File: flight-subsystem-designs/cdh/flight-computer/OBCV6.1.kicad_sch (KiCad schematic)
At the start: 32 parts, among them J1 Conn_01x03, J2 Conn_01x03, J3 Conn_01x03, J4 Conn_01x03, J5 Conn_01x03, J6 Conn_01x03, J7 Conn_02x26_Odd_Even, J8 Conn_02x26_Odd_Even, U1 BEAGLEBONEBLACK, U3 TCAN337G, U4 MCP7940N-xSN, U6 MAX706RESA+T, U7 TMP36xS

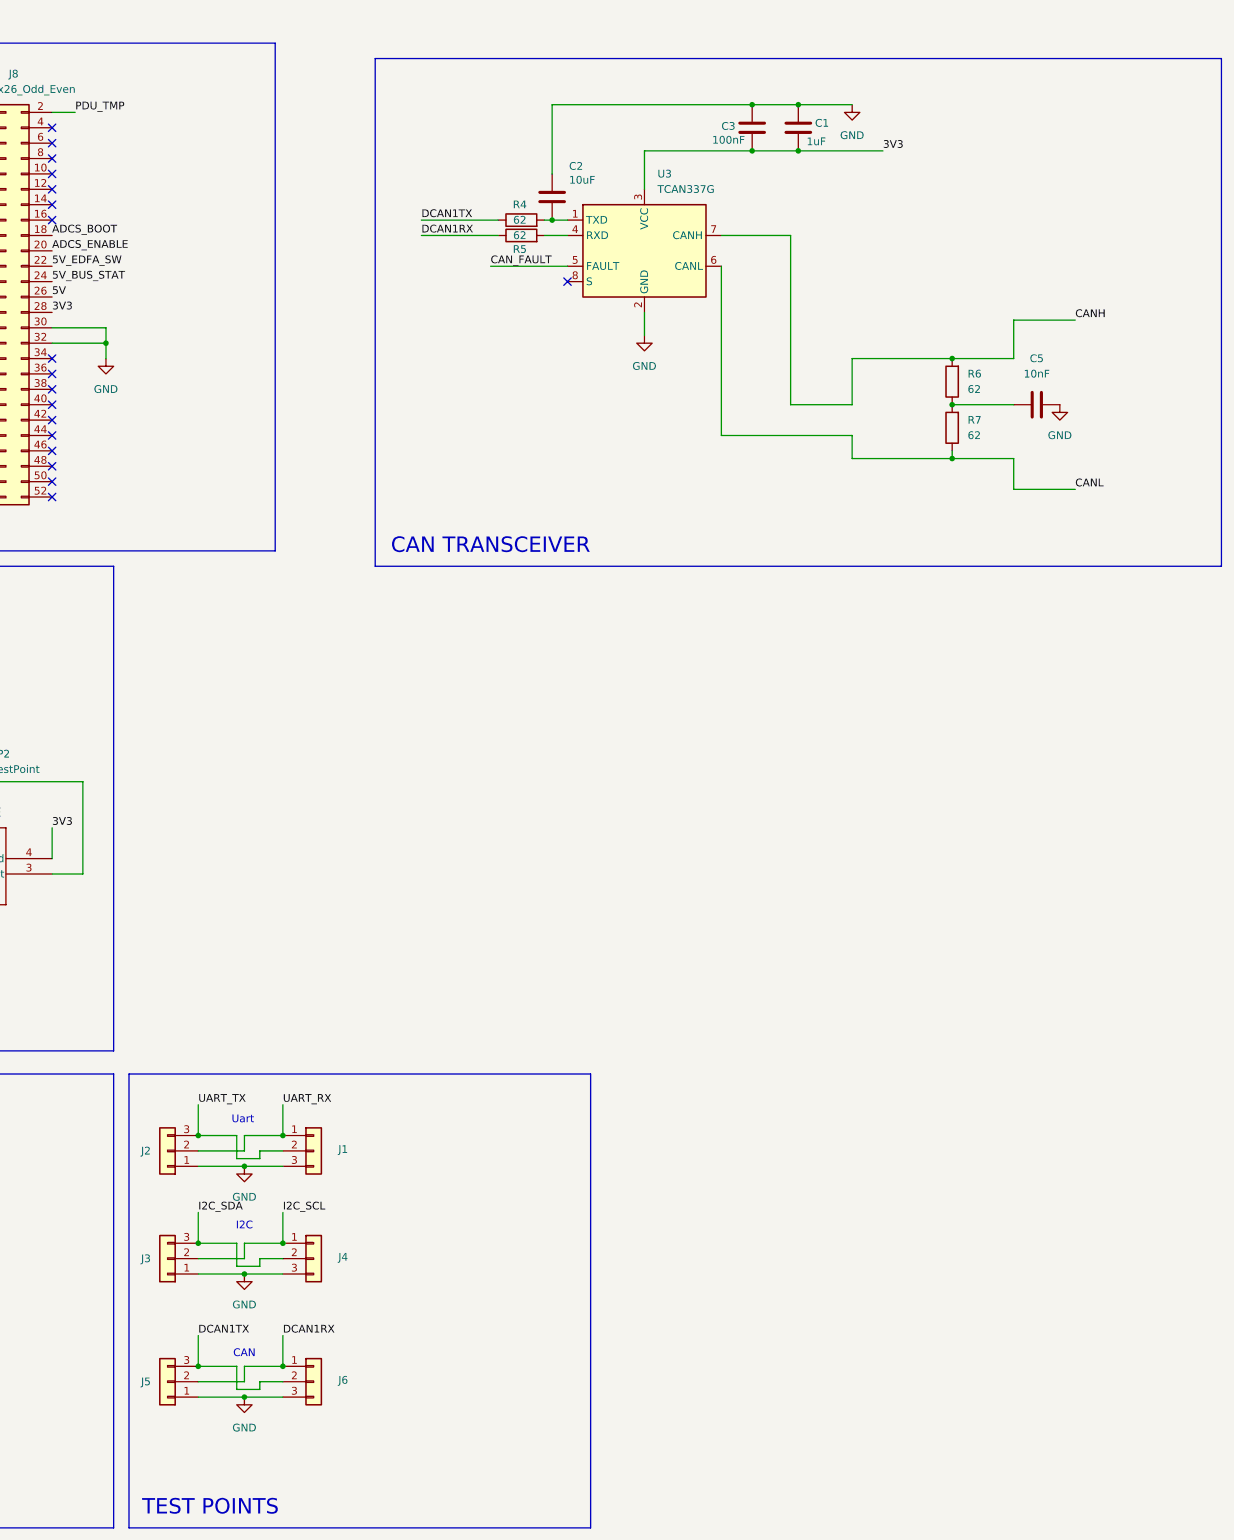
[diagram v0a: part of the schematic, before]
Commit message: Added grounded mounting holes
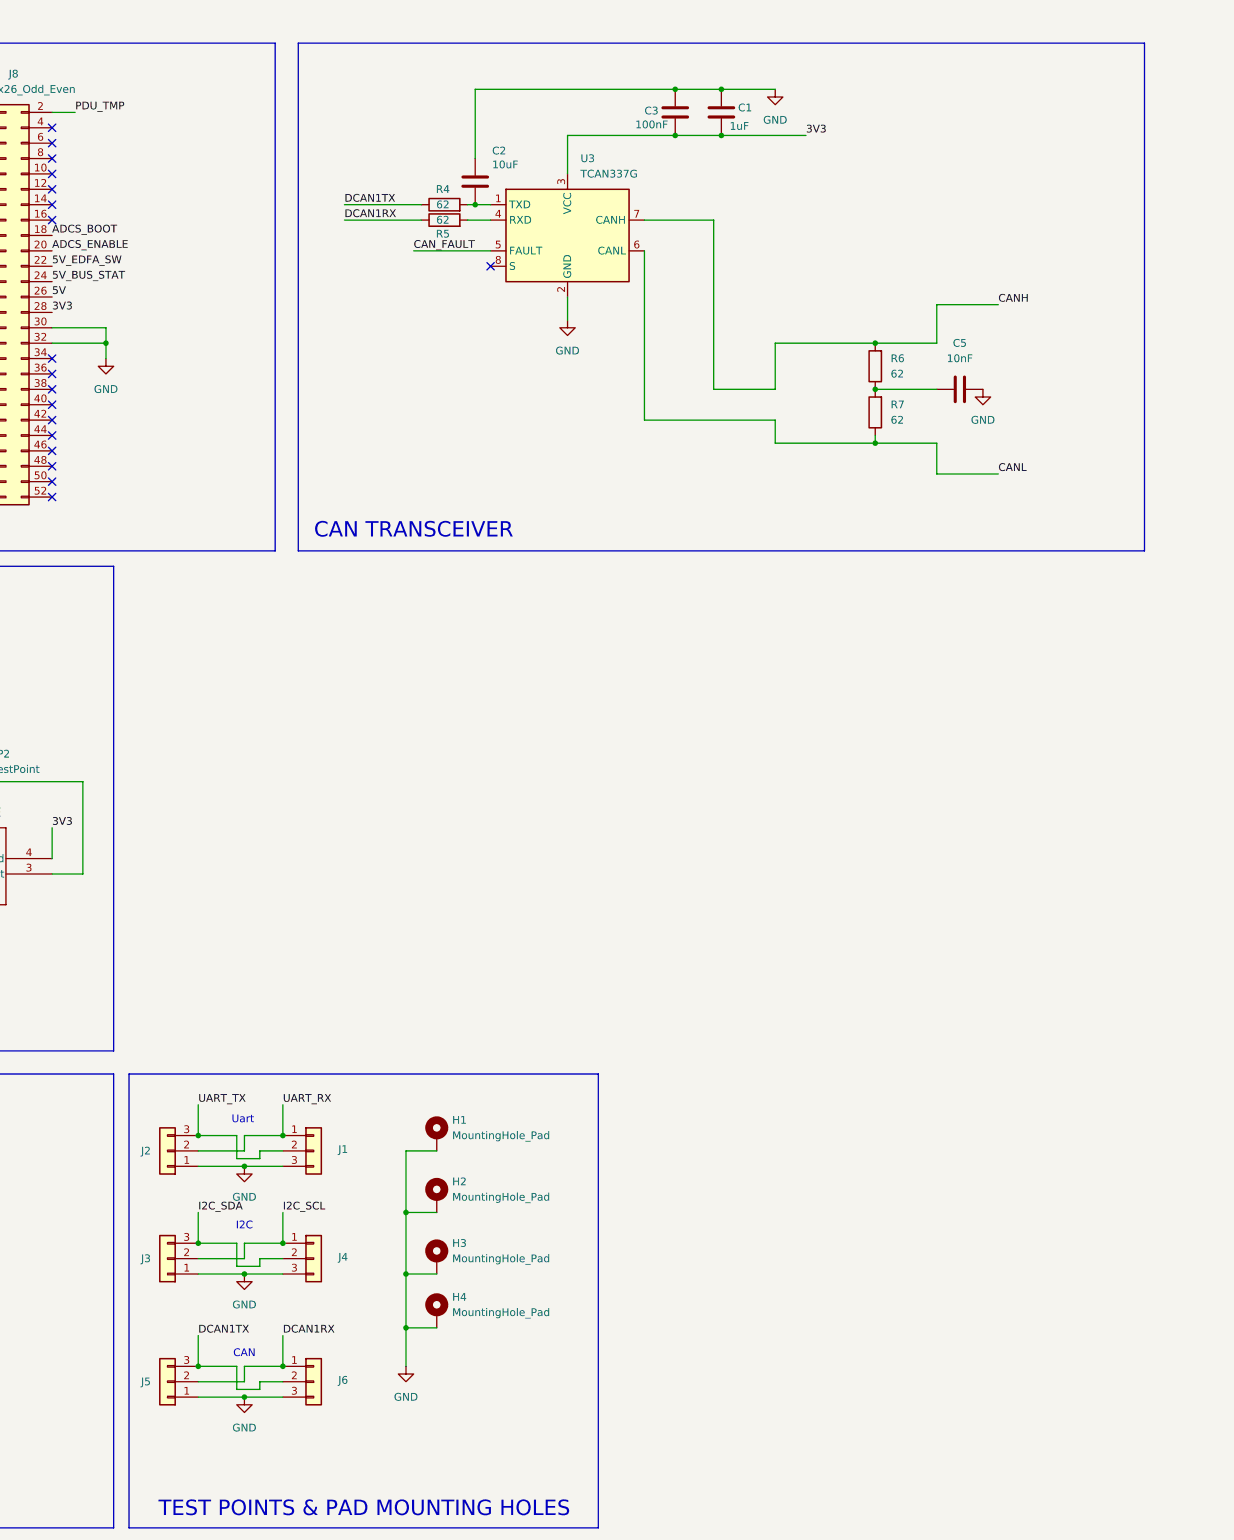
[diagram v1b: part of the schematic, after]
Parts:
- added H1, H2, H3, H4: MountingHole_Pad, symbol Mechanical:MountingHole_Pad
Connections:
- net DGND: now also H1.1, H2.1, H3.1, H4.1
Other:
- note added: "TEST POINTS & PAD MOUNTING HOLES"
- note removed: "TEST POINTS"
- moved on the sheet: C1, C2, C3, C5, R4, R5, R6, R7, U3

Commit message: corrections
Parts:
- J1: footprint Connector_PinHeader_2.54mm:PinHeader_1x03_P2.54mm_Horizontal -> Connector_PinHeader_2.54mm:PinHeader_1x03_P2.54mm_Vertical
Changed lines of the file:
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@@
 			)
 		)
-		(property "Footprint" "Connector_PinHeader_2.54mm:PinHeader_1x03_P2.54mm_Horizontal"
+		(property "Footprint" "Connector_PinHeader_2.54mm:PinHeader_1x03_P2.54mm_Vertical"
 			(at 264.16 196.85 0)
 			(effects

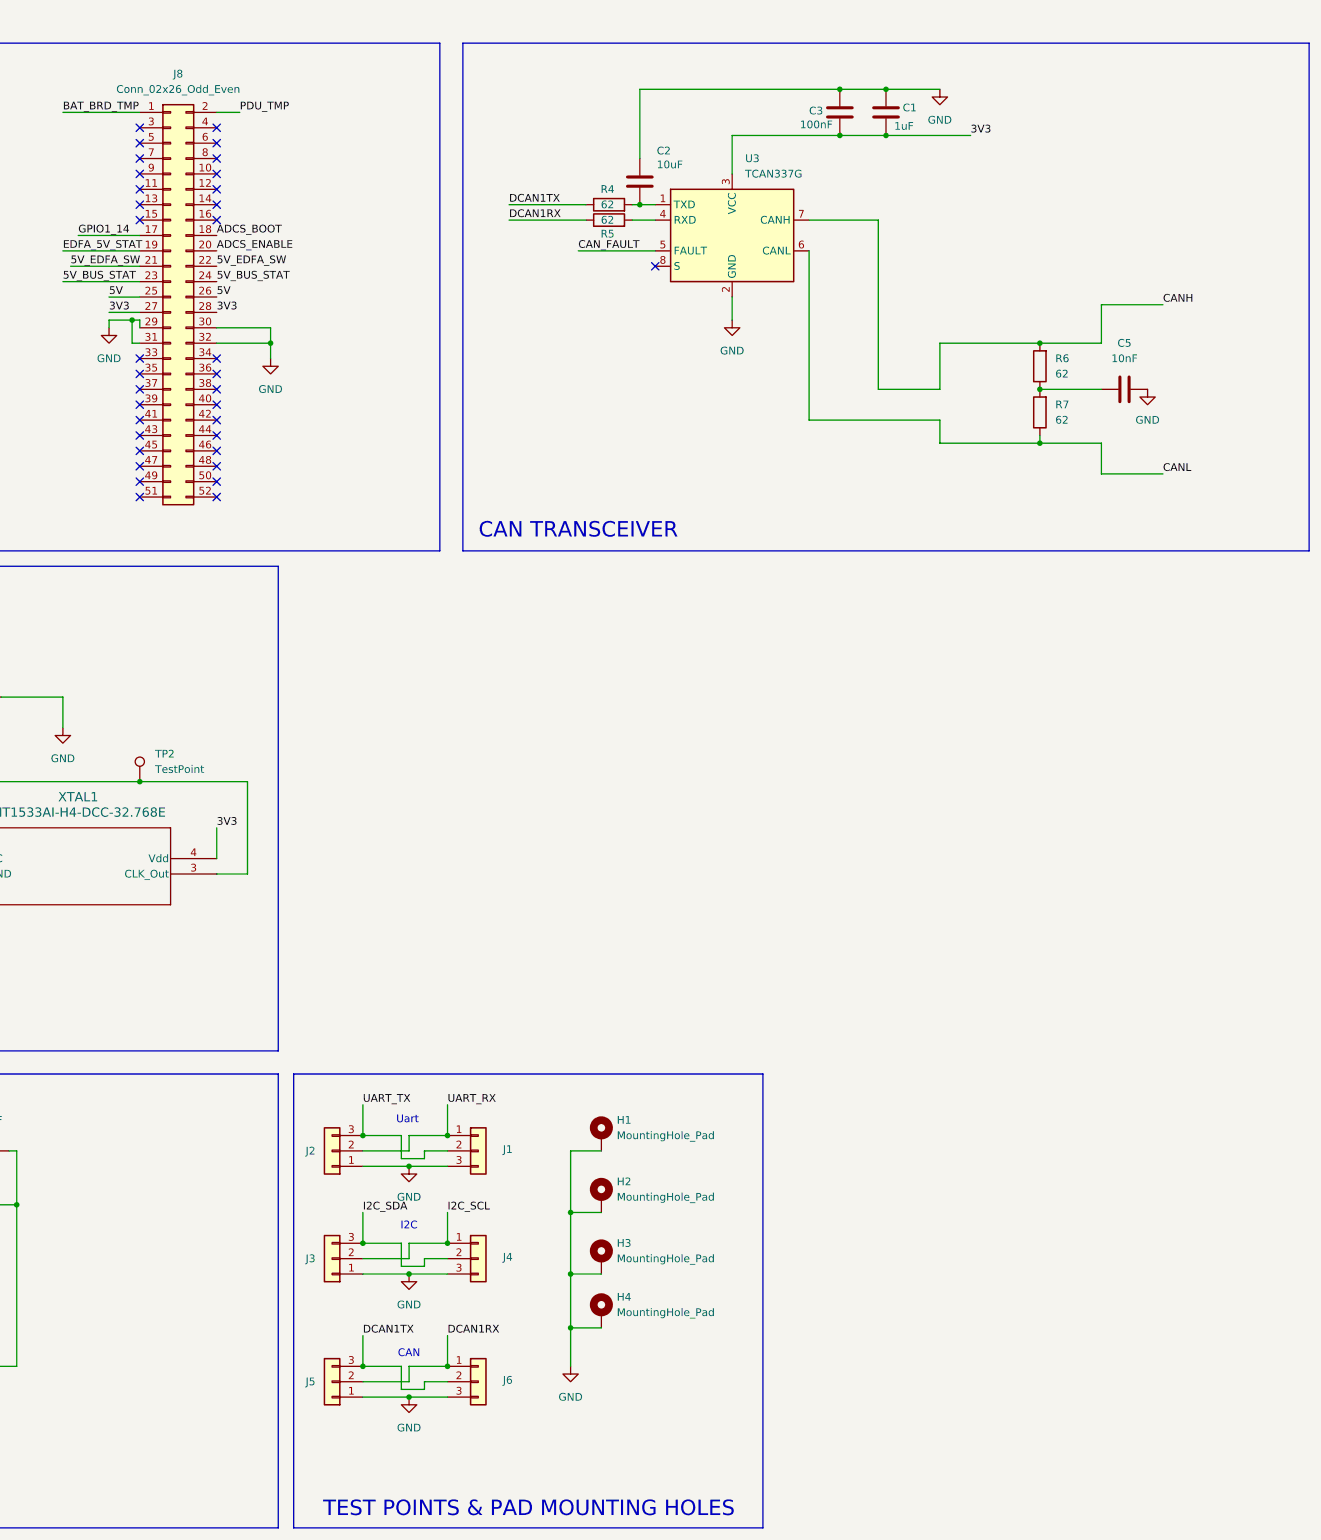
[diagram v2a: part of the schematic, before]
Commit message: Added overvoltage regulation, *check J8*
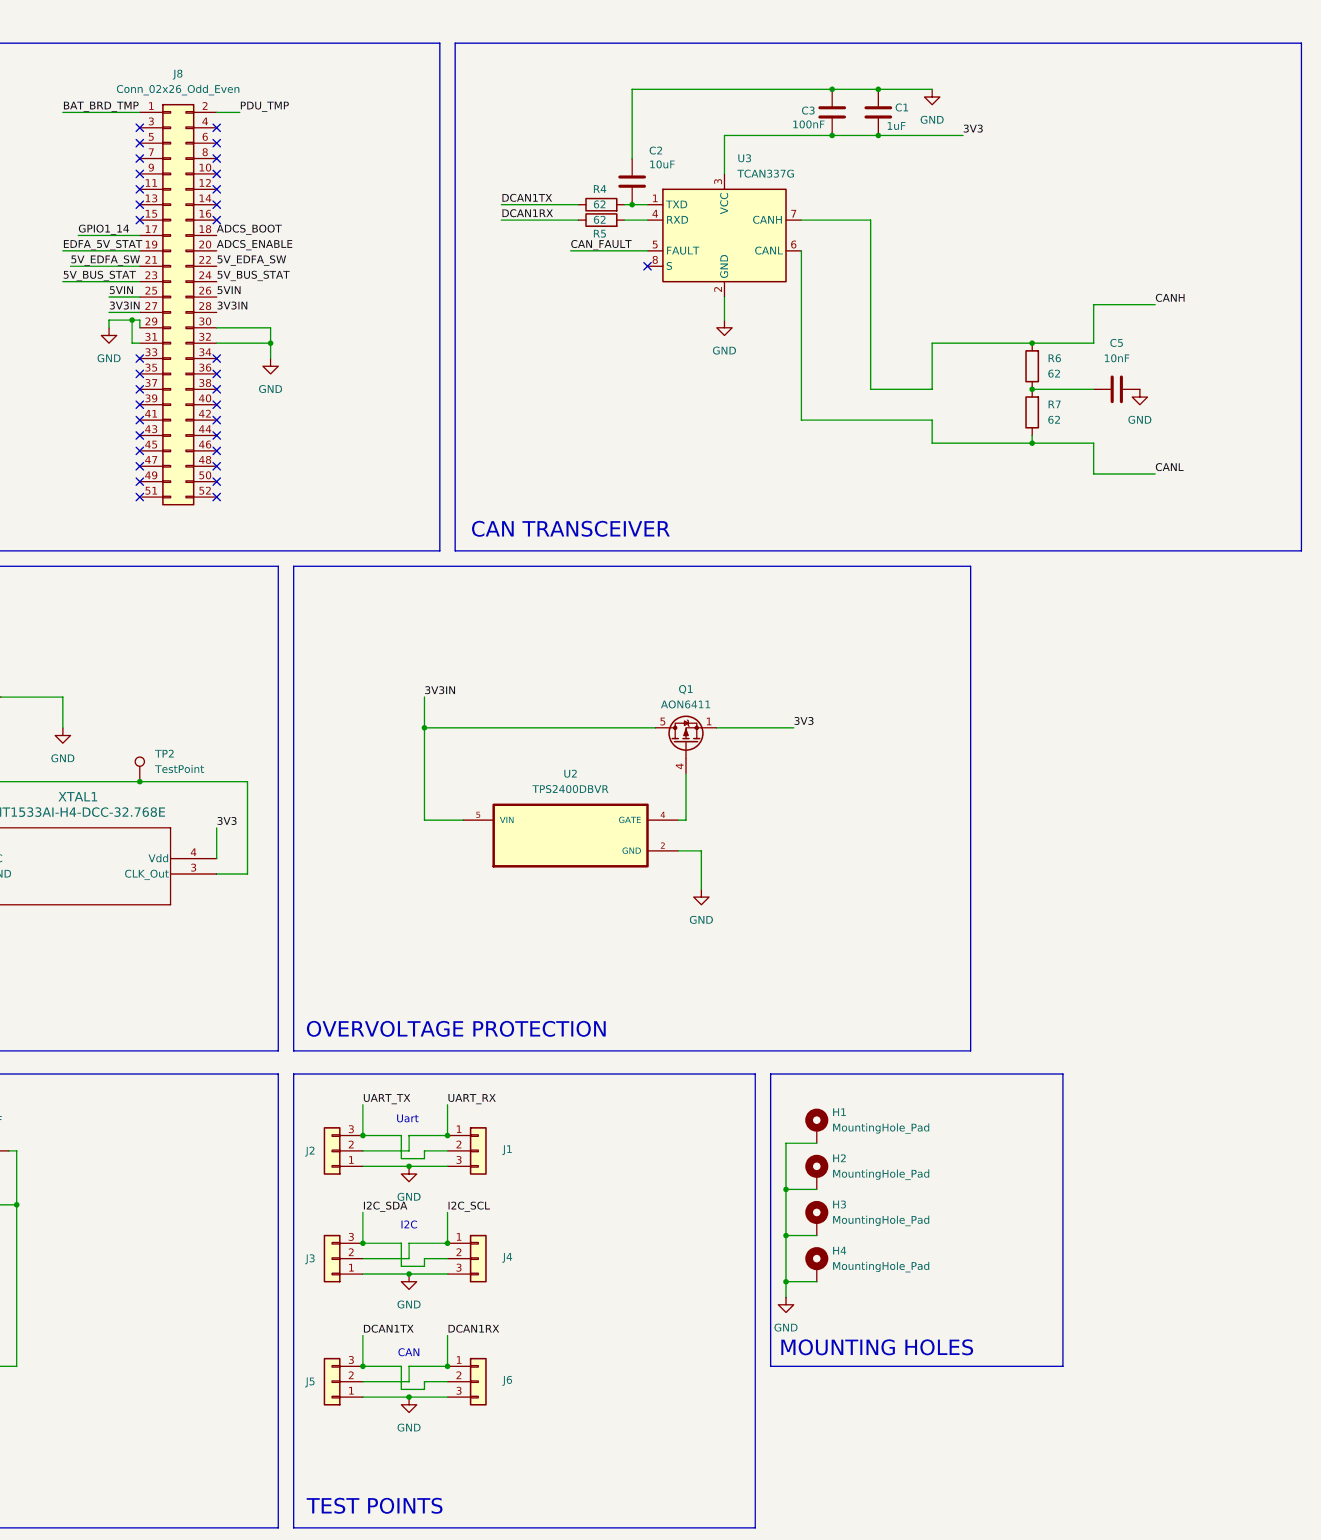
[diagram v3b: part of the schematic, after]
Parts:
- added Q1: AON6411, Package_DFN_QFN:AO_DFN-8-1EP_5.55x5.2mm_P1.27mm_EP4.12x4.6mm, symbol Transistor_FET:AON6411
- added U2: TPS2400DBVR, Footprints:SOT95P280X145-5N, symbol TPS2400DBVR:TPS2400DBVR
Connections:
- net DGND: now also U2.2 (GND)
- net SYS_5V: no longer J8.25 (Pin_25), J8.26 (Pin_26)
- net VDD_3V3B: now also Q1.1 (S), Q1.2 (S), Q1.3 (S); no longer J8.27 (Pin_27), J8.28 (Pin_28)
- new net: Q1.4 (G), U2.4 (GATE)
- new net 3V3IN: J8.27 (Pin_27), J8.28 (Pin_28), Q1.5 (D), U2.5 (VIN)
- new net 5VIN: J8.25 (Pin_25), J8.26 (Pin_26)
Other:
- note added: "MOUNTING HOLES"
- note added: "OVERVOLTAGE PROTECTION"
- note added: "TEST POINTS"
- note removed: "TEST POINTS & PAD MOUNTING HOLES"
- moved on the sheet: C1, C2, C3, C5, R4, R5, R6, R7, U3
